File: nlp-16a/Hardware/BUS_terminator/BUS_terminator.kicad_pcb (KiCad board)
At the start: 2 copper layers, 209.6 x 154.9 mm, 55 parts, among them J1 Conn_02x20_Odd_Even, J2 Conn_02x20_Odd_Even, J3 Conn_02x20_Odd_Even, J4 Conn_02x10_Odd_Even, J5 Screw_Terminal_01x02, J6 Conn_02x16_Odd_Even, J7 Conn_02x16_Odd_Even, U1 CD74HC00, U10 CD74HC245, U11 CD74HC00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

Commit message: アキュムレータ更新
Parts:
- U10, U9: value CD74HC245 -> 74HCT541
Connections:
- U10 pad 11: IN0 -> IO_BUS0
- U10 pad 12: IN1 -> IO_BUS1
- U10 pad 13: IN2 -> IO_BUS2
- U10 pad 14: IN3 -> IO_BUS3
- U10 pad 15: IN4 -> IO_BUS4
- U10 pad 16: IN5 -> IO_BUS5
- U10 pad 17: IN6 -> IO_BUS6
- U10 pad 18: IN7 -> IO_BUS7
- U10 pad 2: IO_BUS7 -> IN7
- U10 pad 3: IO_BUS6 -> IN6
- U10 pad 4: IO_BUS5 -> IN5
- U10 pad 5: IO_BUS4 -> IN4
- U10 pad 6: IO_BUS3 -> IN3
- U10 pad 7: IO_BUS2 -> IN2
- U10 pad 8: IO_BUS1 -> IN1
- U10 pad 9: IO_BUS0 -> IN0
- U9 pad 11: IN8 -> IO_BUS8
- U9 pad 12: IN9 -> IO_BUS9
- U9 pad 13: IN10 -> IO_BUS10
- U9 pad 14: IN11 -> IO_BUS11
- U9 pad 15: IN12 -> IO_BUS12
- U9 pad 16: IN13 -> IO_BUS13
- U9 pad 17: IN14 -> IO_BUS14
- U9 pad 18: IN15 -> IO_BUS15
- U9 pad 2: IO_BUS15 -> IN15
- U9 pad 3: IO_BUS14 -> IN14
- U9 pad 4: IO_BUS13 -> IN13
- U9 pad 5: IO_BUS12 -> IN12
- U9 pad 6: IO_BUS11 -> IN11
- U9 pad 7: IO_BUS10 -> IN10
- U9 pad 8: IO_BUS9 -> IN9
- U9 pad 9: IO_BUS8 -> IN8
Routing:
- net IN15: track 61.2 -> 79.1 mm
- net IN12: track 61.2 -> 70.6 mm
- net IN11: track 61.2 -> 70.6 mm
- net IN13: track 61.2 -> 70.6 mm
- net IN14: track 61.2 -> 69.7 mm
- net IN10: track 61.2 -> 69.3 mm
- net IN9: track 64.6 -> 71.5 mm
- net IN8: track 68.4 -> 75.3 mm
- net IN2: track 86.2 -> 93.1 mm
- net IN6: track 86.2 -> 93.1 mm
- net IN4: track 86.2 -> 93.1 mm
- net IN1: track 86.2 -> 93.1 mm
- net IN0: track 86.2 -> 93.1 mm
- net IN7: track 86.2 -> 93.1 mm
- net IN3: track 86.2 -> 93.1 mm
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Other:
- board text added: "NLP-16A BUS terminator v1.0 S/N:006-0001"
- board text removed: "NLP-16A ALU v1.0 type-C S/N:■■■-■■■■"

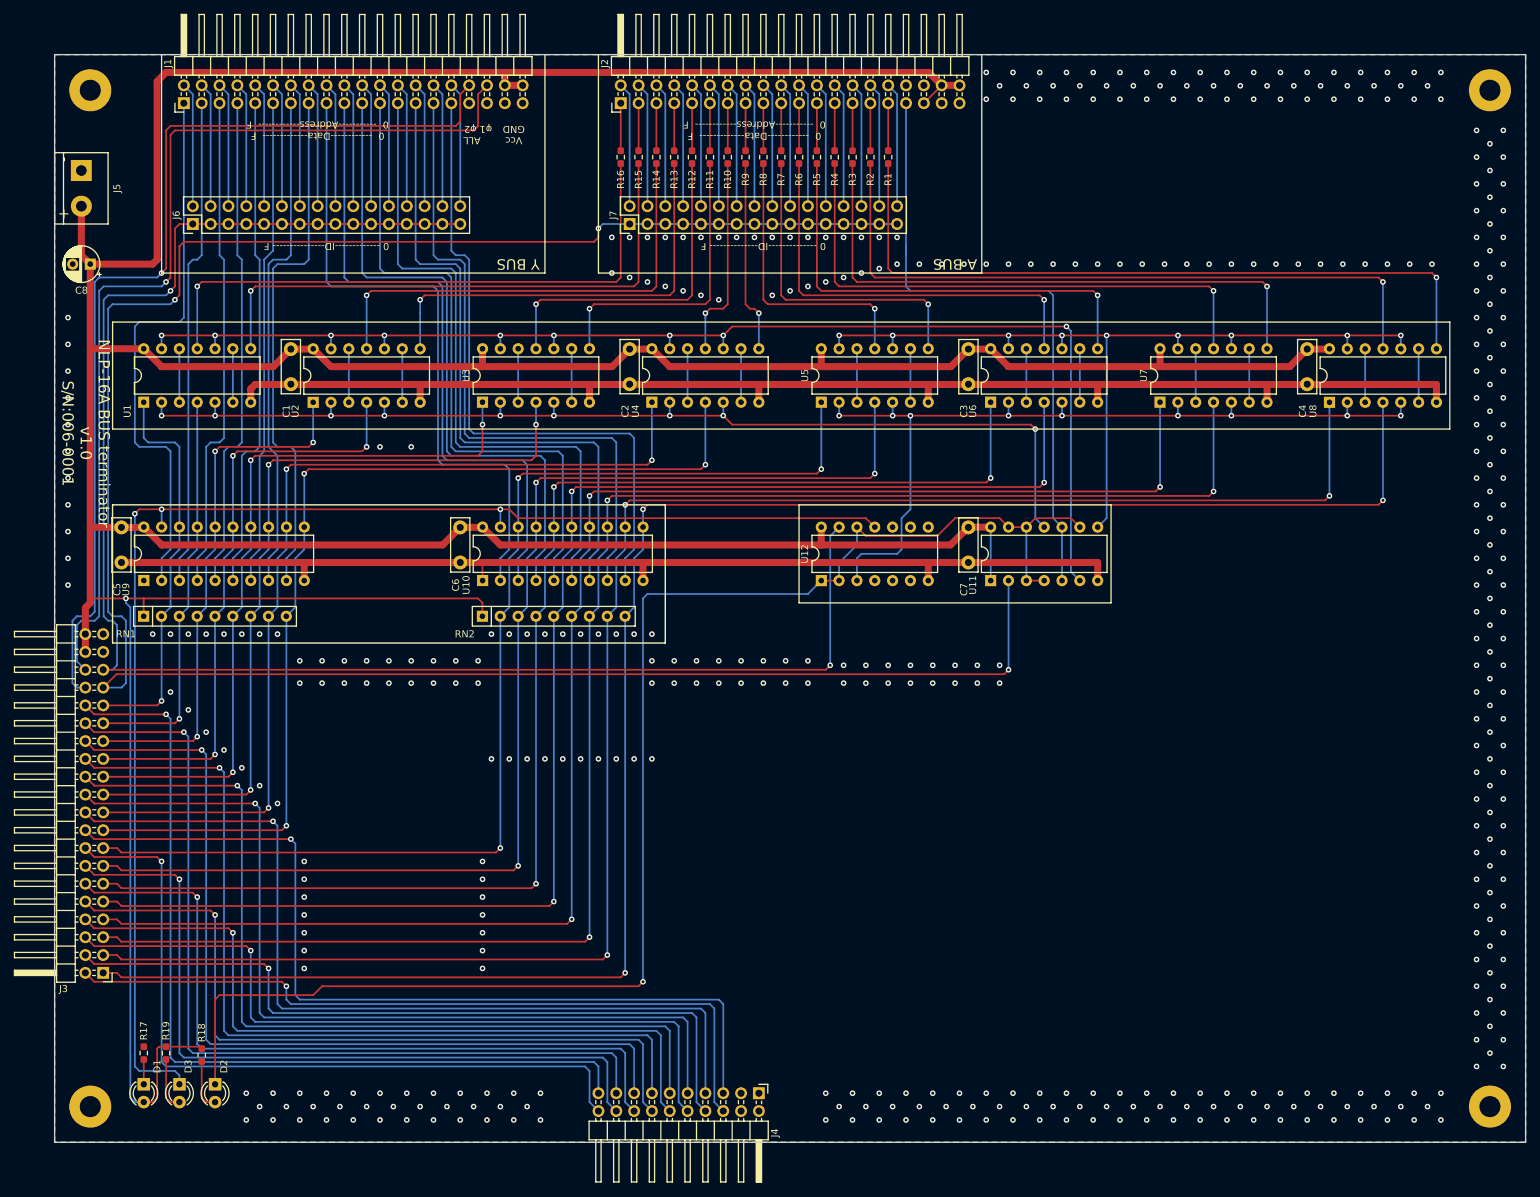
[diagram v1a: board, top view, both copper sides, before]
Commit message: バスターミネータのDMA機能は不要と判断したので削除．必要ならば外部回路で実現するように
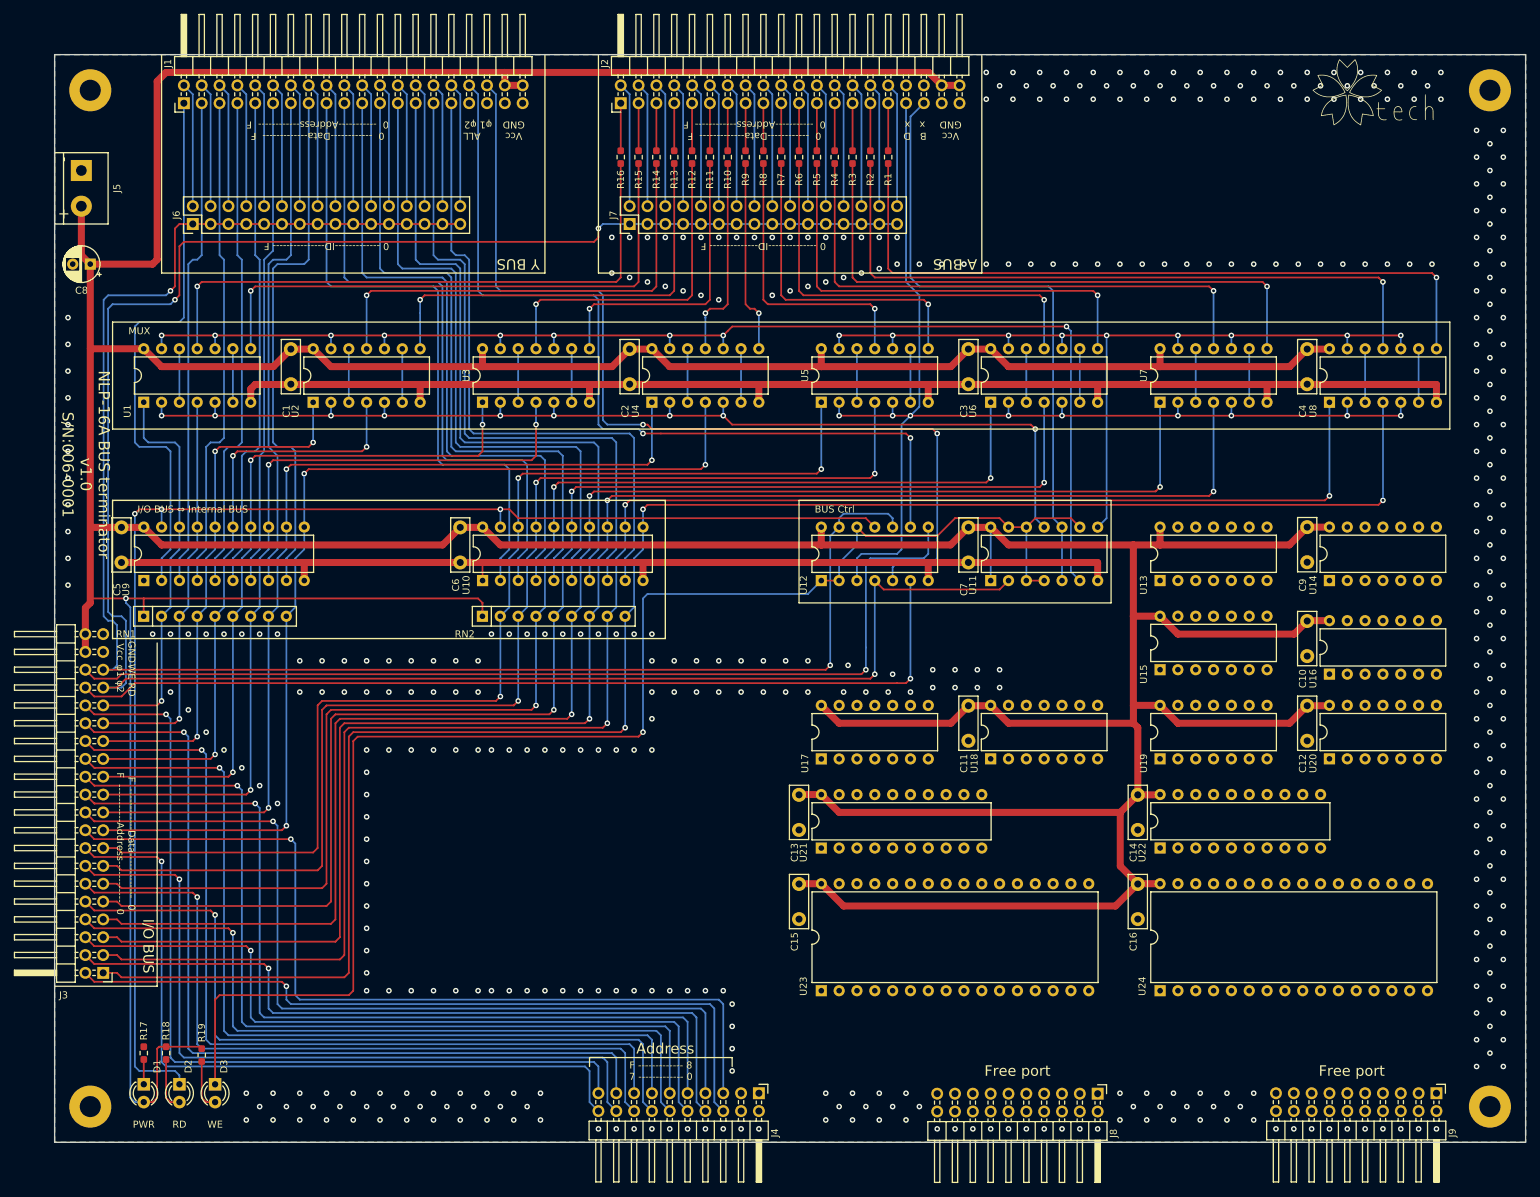
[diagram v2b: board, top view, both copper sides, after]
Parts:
- added C10: C, Capacitor_THT:C_Disc_D7.5mm_W2.5mm_P5.00mm, F.Cu at (210.8, 115.0)
- added C11: C, Capacitor_THT:C_Disc_D7.5mm_W2.5mm_P5.00mm, F.Cu at (162.6, 127.0)
- added C12: C, Capacitor_THT:C_Disc_D7.5mm_W2.5mm_P5.00mm, F.Cu at (210.8, 127.0)
- added C13: C, Capacitor_THT:C_Disc_D7.5mm_W2.5mm_P5.00mm, F.Cu at (138.4, 139.7)
- added C14: C, Capacitor_THT:C_Disc_D7.5mm_W2.5mm_P5.00mm, F.Cu at (186.7, 139.7)
- added C15: C, Capacitor_THT:C_Disc_D7.5mm_W2.5mm_P5.00mm, F.Cu at (138.4, 152.4)
- added C16: C, Capacitor_THT:C_Disc_D7.5mm_W2.5mm_P5.00mm, F.Cu at (186.7, 152.4)
- added C9: C, Capacitor_THT:C_Disc_D7.5mm_W2.5mm_P5.00mm, F.Cu at (210.8, 101.6)
- added G***: LOGO, LOGO, F.Cu at (221.0, 40.0)
- added J8: Conn_02x10_Odd_Even, Connector_PinHeader_2.54mm:PinHeader_2x10_P2.54mm_Horizontal, F.Cu at (181.0, 182.3)
- added J9: Conn_02x10_Odd_Even, Connector_PinHeader_2.54mm:PinHeader_2x10_P2.54mm_Horizontal, F.Cu at (229.2, 182.2)
- added U13: CD74HC00, Package_DIP:DIP-14_W7.62mm, F.Cu at (189.9, 109.2)
- added U14: CD74HC00, Package_DIP:DIP-14_W7.62mm, F.Cu at (214.0, 109.2)
- added U15: CD74HC00, Package_DIP:DIP-14_W7.62mm, F.Cu at (189.9, 121.9)
- added U16: CD74HC00, Package_DIP:DIP-14_W7.62mm, F.Cu at (214.0, 122.5)
- added U17: CD74HC00, Package_DIP:DIP-14_W7.62mm, F.Cu at (141.6, 134.6)
- added U18: CD74HC00, Package_DIP:DIP-14_W7.62mm, F.Cu at (165.7, 134.6)
- added U19: CD74HC00, Package_DIP:DIP-14_W7.62mm, F.Cu at (189.9, 134.6)
- added U20: CD74HC00, Package_DIP:DIP-14_W7.62mm, F.Cu at (214.0, 134.6)
- added U21: 74HCT541, Package_DIP:DIP-20_W7.62mm, F.Cu at (141.6, 147.3)
- added U22: 74HCT541, Package_DIP:DIP-20_W7.62mm, F.Cu at (189.9, 147.3)
- added U23: TC551001, Package_DIP:DIP-32_W15.24mm, F.Cu at (141.6, 167.6)
- added U24: TC551001, Package_DIP:DIP-32_W15.24mm, F.Cu at (189.9, 167.6)
- renumbered D3 to D2, D2 to D3, R19 to R18, R18 to R19
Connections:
- J2 pad 33: Correction -> Data_Correction
- J2 pad 35: VCC -> BUS_Correction
- J3 pad 34: phi2 -> RD_CLK
- J3 pad 36: phi1 -> WR_CLK
- U11 pad 10: Correction -> BUS_Correction
- U11 pad 5: Correction -> BUS_Correction
- U12 pad 10: GND -> Y_SEL
- U12 pad 3: Net-(U12-Pad3) -> Data_Correction
- U12 pad 4: GND -> A_SEL
- U12 pad 5: GND -> phi1
- U12 pad 6: unconnected-(U12-Pad6) -> RD_CLK
- U12 pad 8: unconnected-(U12-Pad8) -> WR_CLK
- U12 pad 9: GND -> phi2
- U5 pad 2: Net-(U12-Pad3) -> Data_Correction
- U5 pad 5: Net-(U12-Pad3) -> Data_Correction
- U6 pad 2: Net-(U12-Pad3) -> Data_Correction
- U6 pad 5: Net-(U12-Pad3) -> Data_Correction
- U7 pad 2: Net-(U12-Pad3) -> Data_Correction
- U7 pad 5: Net-(U12-Pad3) -> Data_Correction
- U8 pad 2: Net-(U12-Pad3) -> Data_Correction
- U8 pad 5: Net-(U12-Pad3) -> Data_Correction
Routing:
- net VCC: track 708.1 -> 1019.6 mm
- net Data_Correction: track 0.00 -> 170.8 mm, vias 0 -> 9
- net WR_CLK: track 0.00 -> 140.7 mm, vias 0 -> 1
- net RD_CLK: track 0.00 -> 133.1 mm, vias 0 -> 1
- net Net-(U12-Pad3): track 125.0 -> 0.00 mm, vias 9 -> 0
- net Correction: track 90.0 -> 0.00 mm
- net BUS_Correction: track 0.00 -> 88.5 mm
- net phi2: track 140.4 -> 123.2 mm, vias 1 -> 2
- net Y_SEL: track 239.6 -> 250.3 mm
- net A_SEL: track 323.6 -> 325.0 mm
- net phi1: track 138.8 -> 137.7 mm, vias 1 -> 2
- net IO_BUS4: track 203.5 -> 202.8 mm
- net IO_BUS7: track 164.1 -> 163.4 mm
- net IO_BUS6: track 174.3 -> 173.5 mm
- net IO_BUS2: track 232.7 -> 232.0 mm
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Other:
- board text added: "Address"
- board text added: "B D x x"
- board text added: "BUS Ctrl"
- board text added: "F ------------- 8 7 ------------- 0"
- board text added: "F ------------Data------------- 0 F -----------Address------------ 0"
- board text added: "Free port"
- board text added: "GND Vcc"
- board text added: "I/O BUS"
- board text added: "I/O BUS ⇔ Internal BUS"
- board text added: "MUX"
- board text added: "PWR"
- board text added: "RD"
- board text added: "WE"
- board text added: "WE RD φ1 φ2"

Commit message: v1.1全ガーバーを更新
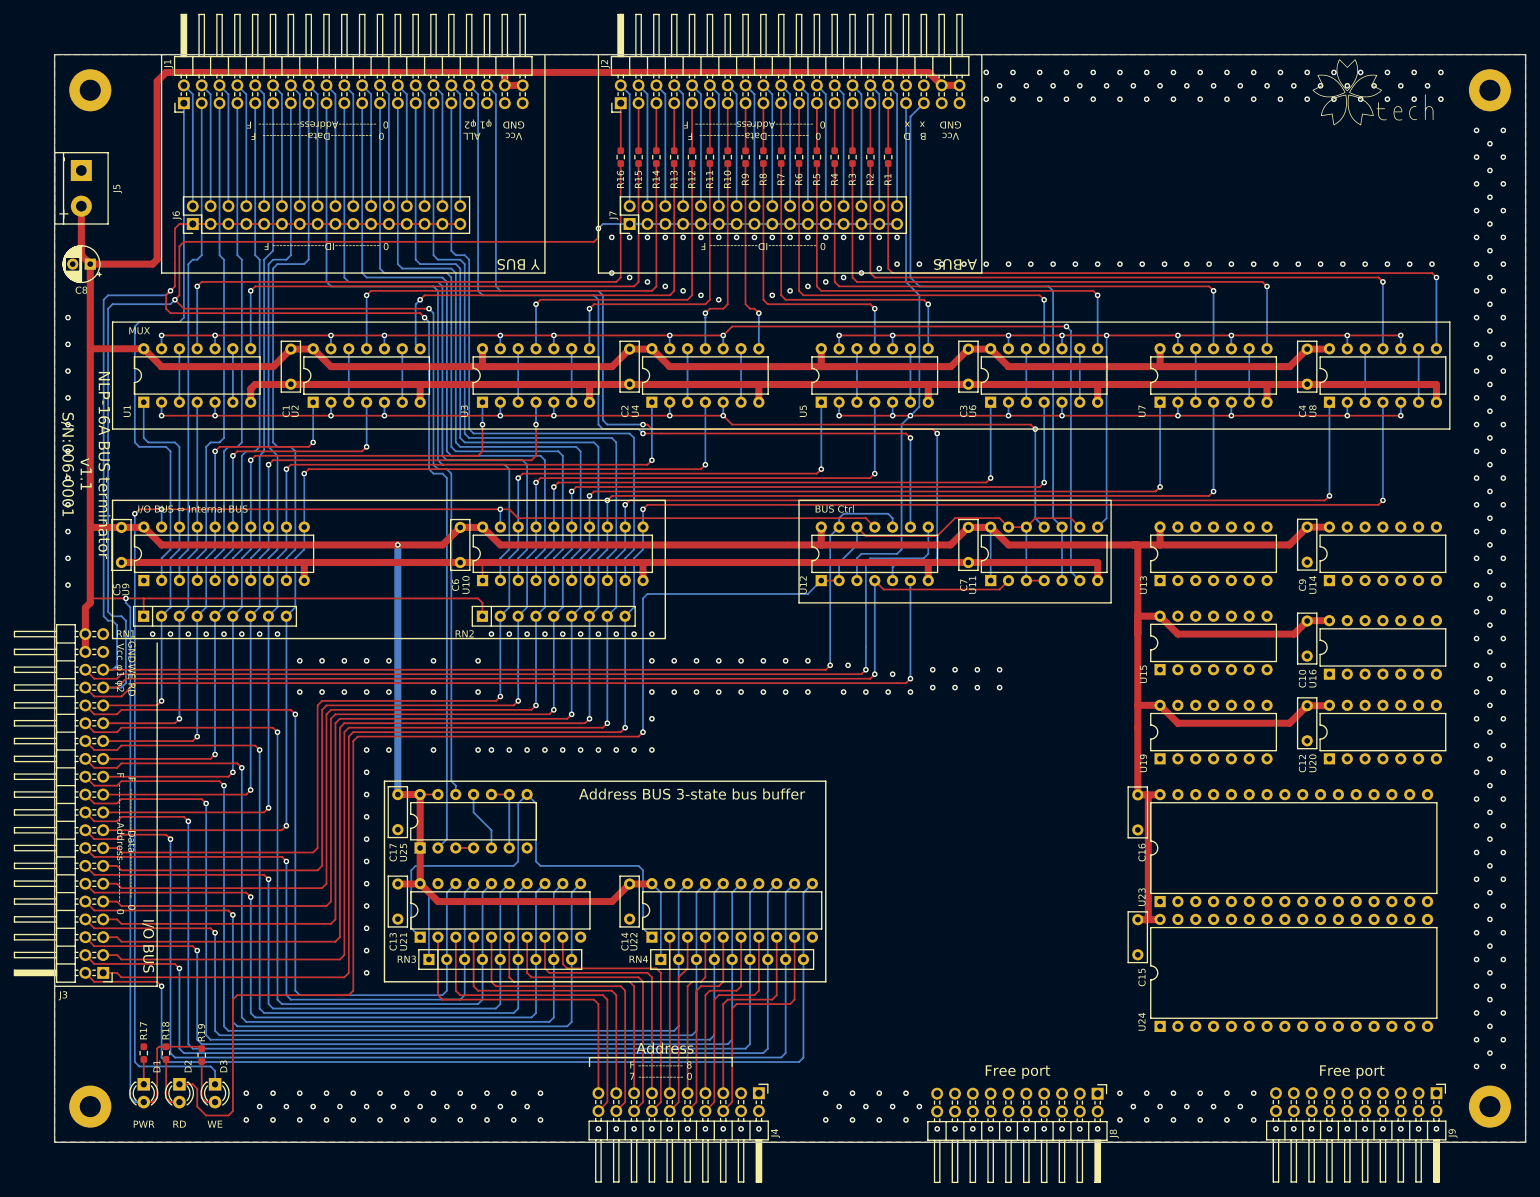
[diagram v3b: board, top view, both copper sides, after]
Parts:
- removed C11: C, Capacitor_THT:C_Disc_D7.5mm_W2.5mm_P5.00mm
- removed U17, U18: CD74HC00, Package_DIP:DIP-14_W7.62mm
- added C17: C, Capacitor_THT:C_Disc_D7.0mm_W2.5mm_P5.00mm, F.Cu at (81.3, 139.7)
- added RN3: R_Network08, Resistor_THT:R_Array_SIP9, F.Cu at (85.7, 163.2)
- added RN4: R_Network08, Resistor_THT:R_Array_SIP9, F.Cu at (118.7, 163.2)
- added U25: CD74HC00, Package_DIP:DIP-14_W7.62mm, F.Cu at (84.5, 147.3)
- C1, C10, C12, C13, C14, C15, C16, C2, C3, C4, C5, C6, C7, C9: footprint Capacitor_THT:C_Disc_D7.5mm_W2.5mm_P5.00mm -> Capacitor_THT:C_Disc_D7.0mm_W2.5mm_P5.00mm
- moved U22 73.5 mm to (117.5, 160.0)
- moved C14 73.5 mm to (114.3, 152.4)
- moved C13 58.5 mm to (81.3, 152.4)
- moved U21 58.5 mm to (84.5, 160.0)
- moved U23 49.9 mm to (189.9, 154.9)
- moved C15 48.5 mm to (186.7, 157.5)
- moved C16 12.7 mm to (186.7, 139.7)
- moved U24 5.09 mm to (189.9, 172.7)
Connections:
- J3 pad 10: Address4 -> Address_out4
- J3 pad 12: Address5 -> Address_out5
- J3 pad 14: Address6 -> Address_out6
- J3 pad 16: Address7 -> Address_out7
- J3 pad 18: Address8 -> Address_out8
- J3 pad 2: Address0 -> Address_out0
- J3 pad 20: Address9 -> Address_out9
- J3 pad 22: Address10 -> Address_out10
- J3 pad 24: Address11 -> Address_out11
- J3 pad 26: Address12 -> Address_out12
- J3 pad 28: Address13 -> Address_out13
- J3 pad 30: Address14 -> Address_out14
- J3 pad 32: Address15 -> Address_out15
- J3 pad 4: Address1 -> Address_out1
- J3 pad 6: Address2 -> Address_out2
- J3 pad 8: Address3 -> Address_out3
- J4 pad 10: Address2 -> Address_in2
- J4 pad 11: Address11 -> Address_in11
- J4 pad 12: Address3 -> Address_in3
- J4 pad 13: Address12 -> Address_in12
- J4 pad 14: Address4 -> Address_in4
- J4 pad 15: Address13 -> Address_in13
- J4 pad 16: Address5 -> Address_in5
- J4 pad 17: Address14 -> Address_in14
- J4 pad 18: Address6 -> Address_in6
- J4 pad 19: Address15 -> Address_in15
- J4 pad 20: Address7 -> Address_in7
- J4 pad 5: Address8 -> Address_in8
- J4 pad 6: Address0 -> Address_in0
- J4 pad 7: Address9 -> Address_in9
- J4 pad 8: Address1 -> Address_in1
- J4 pad 9: Address10 -> Address_in10
- U10 pad 19: Net-(D2-Pad1) -> Net-(D3-Pad1)
- U11 pad 12: Net-(D3-Pad1) -> Net-(D2-Pad1)
- U11 pad 13: Net-(D3-Pad1) -> Net-(D2-Pad1)
- U11 pad 3: Net-(D3-Pad1) -> Net-(D2-Pad1)
- U11 pad 4: Net-(D3-Pad1) -> Net-(D2-Pad1)
- U11 pad 9: Net-(D3-Pad1) -> Net-(D2-Pad1)
- U12 pad 1: Net-(D3-Pad1) -> Net-(D2-Pad1)
- U12 pad 11: Net-(D2-Pad1) -> Net-(D3-Pad1)
- U12 pad 12: Net-(D3-Pad1) -> Net-(D2-Pad1)
- U12 pad 2: Net-(D3-Pad1) -> Net-(D2-Pad1)
- U21 pad 1: unconnected-(U21-Pad1) -> Net-(U21-Pad1)
- U21 pad 11: unconnected-(U21-Pad11) -> Address_out4
- U21 pad 12: unconnected-(U21-Pad12) -> Address_out12
- U21 pad 13: unconnected-(U21-Pad13) -> Address_out5
- U21 pad 14: unconnected-(U21-Pad14) -> Address_out13
- U21 pad 15: unconnected-(U21-Pad15) -> Address_out6
- U21 pad 16: unconnected-(U21-Pad16) -> Address_out14
- U21 pad 17: unconnected-(U21-Pad17) -> Address_out7
- U21 pad 18: unconnected-(U21-Pad18) -> Address_out15
- U21 pad 19: unconnected-(U21-Pad19) -> GND
- U21 pad 2: unconnected-(U21-Pad2) -> Address_in15
- U21 pad 3: unconnected-(U21-Pad3) -> Address_in7
- U21 pad 4: unconnected-(U21-Pad4) -> Address_in14
- U21 pad 5: unconnected-(U21-Pad5) -> Address_in6
- U21 pad 6: unconnected-(U21-Pad6) -> Address_in13
- U21 pad 7: unconnected-(U21-Pad7) -> Address_in5
- U21 pad 8: unconnected-(U21-Pad8) -> Address_in12
- U21 pad 9: unconnected-(U21-Pad9) -> Address_in4
- U22 pad 1: unconnected-(U22-Pad1) -> Net-(U21-Pad1)
- U22 pad 11: unconnected-(U22-Pad11) -> Address_out0
- U22 pad 12: unconnected-(U22-Pad12) -> Address_out8
- U22 pad 13: unconnected-(U22-Pad13) -> Address_out1
- U22 pad 14: unconnected-(U22-Pad14) -> Address_out9
- U22 pad 15: unconnected-(U22-Pad15) -> Address_out2
- U22 pad 16: unconnected-(U22-Pad16) -> Address_out10
- U22 pad 17: unconnected-(U22-Pad17) -> Address_out3
- U22 pad 18: unconnected-(U22-Pad18) -> Address_out11
- U22 pad 19: unconnected-(U22-Pad19) -> GND
- U22 pad 2: unconnected-(U22-Pad2) -> Address_in11
- U22 pad 3: unconnected-(U22-Pad3) -> Address_in3
- U22 pad 4: unconnected-(U22-Pad4) -> Address_in10
- U22 pad 5: unconnected-(U22-Pad5) -> Address_in2
- U22 pad 6: unconnected-(U22-Pad6) -> Address_in9
- U22 pad 7: unconnected-(U22-Pad7) -> Address_in1
- U22 pad 8: unconnected-(U22-Pad8) -> Address_in8
- U22 pad 9: unconnected-(U22-Pad9) -> Address_in0
- U9 pad 19: Net-(D2-Pad1) -> Net-(D3-Pad1)
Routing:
- net Address_out8: track 0.00 -> 156.5 mm, vias 0 -> 1
- net Address_out9: track 0.00 -> 151.4 mm, vias 0 -> 1
- net Address_out10: track 0.00 -> 146.3 mm, vias 0 -> 1
- net Address_out11: track 0.00 -> 141.2 mm, vias 0 -> 1
- net Address_out0: track 0.00 -> 139.1 mm, vias 0 -> 1
- net Address_out1: track 0.00 -> 134.0 mm, vias 0 -> 1
- net Address_out2: track 0.00 -> 128.9 mm, vias 0 -> 1
- net Address10: track 126.5 -> 0.00 mm, vias 1 -> 0
- net Address8: track 126.5 -> 0.00 mm, vias 1 -> 0
- net Address14: track 126.5 -> 0.00 mm, vias 1 -> 0
- net Address12: track 126.5 -> 0.00 mm, vias 1 -> 0
- net Address11: track 126.5 -> 0.00 mm, vias 1 -> 0
- net Address15: track 126.5 -> 0.00 mm, vias 1 -> 0
- net Address13: track 126.5 -> 0.00 mm, vias 1 -> 0
- net Address9: track 126.5 -> 0.00 mm, vias 1 -> 0
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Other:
- board text added: "Address BUS 3-state bus buffer"
- board text added: "NLP-16A BUS terminator v1.1 S/N:006-0001"
- board text removed: "NLP-16A BUS terminator v1.0 S/N:006-0001"
